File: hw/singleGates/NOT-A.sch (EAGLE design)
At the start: 3 parts, among them Q1 BC817

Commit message: Basic cleanups
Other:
- moved on the sheet: Q1, R1, R2
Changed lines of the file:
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@@
 <sheet>
 <plain>
-<wire x1="20.32" y1="-12.7" x2="-10.16" y2="-12.7" width="0.4064" layer="97" style="longdash"/>
-<wire x1="-10.16" y1="12.7" x2="-10.16" y2="-12.7" width="0.4064" layer="97" style="longdash"/>
-<wire x1="20.32" y1="12.7" x2="20.32" y2="-12.7" width="0.4064" layer="97" style="longdash"/>
-<wire x1="-10.16" y1="12.7" x2="20.32" y2="12.7" width="0.4064" layer="97" style="longdash"/>
-<text x="13.208" y="9.144" size="2.54" layer="97" ratio="12">NOT</text>
+<wire x1="20.32" y1="-10.16" x2="-10.16" y2="-10.16" width="0.4064" layer="97" style="longdash"/>
+<wire x1="-10.16" y1="15.24" x2="-10.16" y2="-10.16" width="0.4064" layer="97" style="longdash"/>
+<wire x1="20.32" y1="15.24" x2="20.32" y2="-10.16" width="0.4064" layer="97" style="longdash"/>
+<wire x1="-10.16" y1="15.24" x2="20.32" y2="15.24" width="0.4064" layer="97" style="longdash"/>
+<text x="13.208" y="11.684" size="2.54" layer="97" ratio="12">NOT</text>
 </plain>
 <instances>
-<instance part="R1" gate="G$1" x="0" y="-2.54"/>
-<instance part="R2" gate="G$1" x="5.08" y="7.62"/>
-<instance part="Q1" gate="G$1" x="12.7" y="-2.54" smashed="yes">
-<attribute name="NAME" x="12.7" y="-6.858" size="1.27" layer="95" ratio="12" rot="R180" align="top-left"/>
-<attribute name="VALUE" x="10.16" y="-0.762" size="1.27" layer="96" ratio="12" rot="R180"/>
+<instance part="R1" gate="G$1" x="0" y="0"/>
+<instance part="R2" gate="G$1" x="5.08" y="10.16"/>
+<instance part="Q1" gate="G$1" x="12.7" y="0" smashed="yes">
+<attribute name="NAME" x="12.7" y="-4.318" size="1.27" layer="95" ratio="12" rot="R180" align="top-left"/>
+<attribute name="VALUE" x="10.16" y="1.778" size="1.27" layer="96" ratio="12" rot="R180"/>
 </instance>
 </instances>
@@
 <net name="_VN" class="0">
 <segment>
-<wire x1="-2.54" y1="-10.16" x2="12.7" y2="-10.16" width="0.1524" layer="91"/>
-<wire x1="12.7" y1="-10.16" x2="12.7" y2="-7.62" width="0.1524" layer="91"/>
-<label x="-2.032" y="-12.192" size="1.778" layer="95"/>
-<wire x1="-2.54" y1="-10.16" x2="-2.54" y2="-12.7" width="0.1524" layer="91"/>
+<wire x1="-2.54" y1="-7.62" x2="12.7" y2="-7.62" width="0.1524" layer="91"/>
+<wire x1="12.7" y1="-7.62" x2="12.7" y2="-5.08" width="0.1524" layer="91"/>
+<label x="-2.032" y="-9.652" size="1.778" layer="95"/>
+<wire x1="-2.54" y1="-7.62" x2="-2.54" y2="-10.16" width="0.1524" layer="91"/>
 <pinref part="Q1" gate="G$1" pin="EMITTER"/>
 </segment>
@@
 <segment>
 <pinref part="R1" gate="G$1" pin="2"/>
-<wire x1="5.08" y1="-2.54" x2="7.62" y2="-2.54" width="0.1524" layer="91"/>
+<wire x1="5.08" y1="0" x2="7.62" y2="0" width="0.1524" layer="91"/>
 <pinref part="Q1" gate="G$1" pin="BASE"/>
 </segment>
@@
 <net name="NOT" class="0">
 <segment>
-<wire x1="12.7" y1="2.54" x2="12.7" y2="7.62" width="0.1524" layer="91"/>
-<wire x1="12.7" y1="7.62" x2="15.24" y2="7.62" width="0.1524" layer="91"/>
-<wire x1="15.24" y1="7.62" x2="15.24" y2="-2.54" width="0.1524" layer="91"/>
-<wire x1="15.24" y1="-2.54" x2="20.32" y2="-2.54" width="0.1524" layer="91"/>
-<label x="15.748" y="-4.572" size="1.778" layer="95"/>
+<wire x1="12.7" y1="5.08" x2="12.7" y2="10.16" width="0.1524" layer="91"/>
+<wire x1="12.7" y1="10.16" x2="15.24" y2="10.16" width="0.1524" layer="91"/>
+<wire x1="15.24" y1="10.16" x2="15.24" y2="0" width="0.1524" layer="91"/>
+<wire x1="15.24" y1="0" x2="20.32" y2="0" width="0.1524" layer="91"/>
+<label x="15.748" y="-2.032" size="1.778" layer="95"/>
 <pinref part="R2" gate="G$1" pin="2"/>
-<wire x1="12.7" y1="7.62" x2="10.16" y2="7.62" width="0.1524" layer="91"/>
-<junction x="12.7" y="7.62"/>
+<wire x1="12.7" y1="10.16" x2="10.16" y2="10.16" width="0.1524" layer="91"/>
+<junction x="12.7" y="10.16"/>
 <pinref part="Q1" gate="G$1" pin="COLLECTOR"/>
 </segment>
@@
 <segment>
 <pinref part="R1" gate="G$1" pin="1"/>
-<wire x1="-5.08" y1="-2.54" x2="-7.62" y2="-2.54" width="0.1524" layer="91"/>
-<wire x1="-7.62" y1="-2.54" x2="-10.16" y2="-2.54" width="0.1524" layer="91"/>
-<label x="-9.652" y="-2.286" size="1.778" layer="95"/>
+<wire x1="-5.08" y1="0" x2="-7.62" y2="0" width="0.1524" layer="91"/>
+<wire x1="-7.62" y1="0" x2="-10.16" y2="0" width="0.1524" layer="91"/>
+<label x="-9.652" y="0.254" size="1.778" layer="95"/>
 </segment>
 </net>
@@
 <segment>
 <pinref part="R2" gate="G$1" pin="1"/>
-<wire x1="0" y1="7.62" x2="-2.54" y2="7.62" width="0.1524" layer="91"/>
-<wire x1="-2.54" y1="7.62" x2="-2.54" y2="12.7" width="0.1524" layer="91"/>
-<label x="-2.54" y="9.652" size="1.778" layer="95" rot="R180"/>
+<wire x1="0" y1="10.16" x2="-2.54" y2="10.16" width="0.1524" layer="91"/>
+<wire x1="-2.54" y1="10.16" x2="-2.54" y2="15.24" width="0.1524" layer="91"/>
+<label x="-2.54" y="12.192" size="1.778" layer="95" rot="R180"/>
 </segment>
 </net>

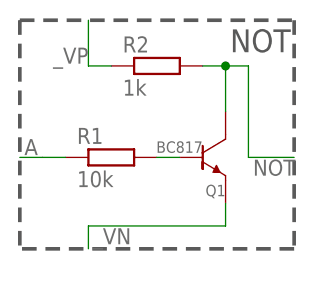
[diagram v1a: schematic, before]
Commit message: fixes some offset and juction issues
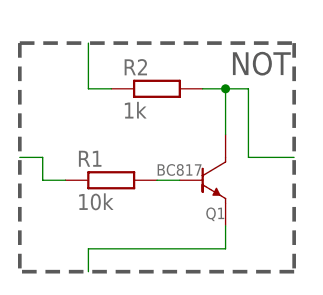
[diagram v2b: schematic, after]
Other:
- moved on the sheet: Q1, R1, R2
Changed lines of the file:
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@@
 <sheet>
 <plain>
-<wire x1="20.32" y1="-10.16" x2="-10.16" y2="-10.16" width="0.4064" layer="97" style="longdash"/>
-<wire x1="-10.16" y1="15.24" x2="-10.16" y2="-10.16" width="0.4064" layer="97" style="longdash"/>
-<wire x1="20.32" y1="15.24" x2="20.32" y2="-10.16" width="0.4064" layer="97" style="longdash"/>
-<wire x1="-10.16" y1="15.24" x2="20.32" y2="15.24" width="0.4064" layer="97" style="longdash"/>
-<text x="13.208" y="11.684" size="2.54" layer="97" ratio="12">NOT</text>
+<wire x1="20.32" y1="-12.7" x2="-10.16" y2="-12.7" width="0.4064" layer="97" style="longdash"/>
+<wire x1="-10.16" y1="12.7" x2="-10.16" y2="-12.7" width="0.4064" layer="97" style="longdash"/>
+<wire x1="20.32" y1="12.7" x2="20.32" y2="-12.7" width="0.4064" layer="97" style="longdash"/>
+<wire x1="-10.16" y1="12.7" x2="20.32" y2="12.7" width="0.4064" layer="97" style="longdash"/>
+<text x="13.208" y="9.144" size="2.54" layer="97" ratio="12">NOT</text>
 </plain>
 <instances>
-<instance part="R1" gate="G$1" x="0" y="0"/>
-<instance part="R2" gate="G$1" x="5.08" y="10.16"/>
-<instance part="Q1" gate="G$1" x="12.7" y="0" smashed="yes">
-<attribute name="NAME" x="12.7" y="-4.318" size="1.27" layer="95" ratio="12" rot="R180" align="top-left"/>
-<attribute name="VALUE" x="10.16" y="1.778" size="1.27" layer="96" ratio="12" rot="R180"/>
+<instance part="R1" gate="G$1" x="0" y="-2.54"/>
+<instance part="R2" gate="G$1" x="5.08" y="7.62"/>
+<instance part="Q1" gate="G$1" x="12.7" y="-2.54" smashed="yes">
+<attribute name="NAME" x="12.7" y="-6.858" size="1.27" layer="95" ratio="12" rot="R180" align="top-left"/>
+<attribute name="VALUE" x="10.16" y="-0.762" size="1.27" layer="96" ratio="12" rot="R180"/>
 </instance>
 </instances>
@@
 <net name="_VN" class="0">
 <segment>
-<wire x1="-2.54" y1="-7.62" x2="12.7" y2="-7.62" width="0.1524" layer="91"/>
-<wire x1="12.7" y1="-7.62" x2="12.7" y2="-5.08" width="0.1524" layer="91"/>
-<label x="-2.032" y="-9.652" size="1.778" layer="95"/>
-<wire x1="-2.54" y1="-7.62" x2="-2.54" y2="-10.16" width="0.1524" layer="91"/>
+<wire x1="-2.54" y1="-10.16" x2="12.7" y2="-10.16" width="0.1524" layer="91"/>
+<wire x1="12.7" y1="-10.16" x2="12.7" y2="-7.62" width="0.1524" layer="91"/>
+<wire x1="-2.54" y1="-10.16" x2="-2.54" y2="-12.7" width="0.1524" layer="91"/>
 <pinref part="Q1" gate="G$1" pin="EMITTER"/>
 </segment>
@@
 <segment>
 <pinref part="R1" gate="G$1" pin="2"/>
-<wire x1="5.08" y1="0" x2="7.62" y2="0" width="0.1524" layer="91"/>
+<wire x1="5.08" y1="-2.54" x2="7.62" y2="-2.54" width="0.1524" layer="91"/>
 <pinref part="Q1" gate="G$1" pin="BASE"/>
 </segment>
@@
 <net name="NOT" class="0">
 <segment>
-<wire x1="12.7" y1="5.08" x2="12.7" y2="10.16" width="0.1524" layer="91"/>
-<wire x1="12.7" y1="10.16" x2="15.24" y2="10.16" width="0.1524" layer="91"/>
-<wire x1="15.24" y1="10.16" x2="15.24" y2="0" width="0.1524" layer="91"/>
+<wire x1="12.7" y1="2.54" x2="12.7" y2="7.62" width="0.1524" layer="91"/>
+<wire x1="12.7" y1="7.62" x2="15.24" y2="7.62" width="0.1524" layer="91"/>
+<wire x1="15.24" y1="7.62" x2="15.24" y2="0" width="0.1524" layer="91"/>
 <wire x1="15.24" y1="0" x2="20.32" y2="0" width="0.1524" layer="91"/>
-<label x="15.748" y="-2.032" size="1.778" layer="95"/>
 <pinref part="R2" gate="G$1" pin="2"/>
-<wire x1="12.7" y1="10.16" x2="10.16" y2="10.16" width="0.1524" layer="91"/>
-<junction x="12.7" y="10.16"/>
+<wire x1="12.7" y1="7.62" x2="10.16" y2="7.62" width="0.1524" layer="91"/>
+<junction x="12.7" y="7.62"/>
 <pinref part="Q1" gate="G$1" pin="COLLECTOR"/>
 </segment>
@@
 <segment>
 <pinref part="R1" gate="G$1" pin="1"/>
-<wire x1="-5.08" y1="0" x2="-7.62" y2="0" width="0.1524" layer="91"/>
+<wire x1="-5.08" y1="-2.54" x2="-7.62" y2="-2.54" width="0.1524" layer="91"/>
+<wire x1="-7.62" y1="-2.54" x2="-7.62" y2="0" width="0.1524" layer="91"/>
 <wire x1="-7.62" y1="0" x2="-10.16" y2="0" width="0.1524" layer="91"/>
-<label x="-9.652" y="0.254" size="1.778" layer="95"/>
 </segment>
 </net>
@@
 <segment>
 <pinref part="R2" gate="G$1" pin="1"/>
-<wire x1="0" y1="10.16" x2="-2.54" y2="10.16" width="0.1524" layer="91"/>
-<wire x1="-2.54" y1="10.16" x2="-2.54" y2="15.24" width="0.1524" layer="91"/>
-<label x="-2.54" y="12.192" size="1.778" layer="95" rot="R180"/>
+<wire x1="0" y1="7.62" x2="-2.54" y2="7.62" width="0.1524" layer="91"/>
+<wire x1="-2.54" y1="7.62" x2="-2.54" y2="12.7" width="0.1524" layer="91"/>
 </segment>
 </net>
